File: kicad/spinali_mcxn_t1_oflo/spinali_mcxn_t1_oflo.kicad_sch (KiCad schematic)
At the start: 0 parts

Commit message: Added Rev-A in MR-MCXN-T1-OFLO
- Added Rev-A in schematic and layout
- Created production files

Signed-off-by: Youri Tils <youri.tils@nxp.com>
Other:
- company: NXP SEMICONDUCTORS B.V. -> ${COMPANY}
- title: MR-MCXN-T1-OFLO -> ${TITLE}
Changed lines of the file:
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@@
 	(paper "A4")
 	(title_block
-		(title "MR-MCXN-T1-OFLO")
-		(date "2025-04-16")
-		(rev "X0")
-		(company "NXP SEMICONDUCTORS B.V.")
-		(comment 3 "DESIGNER: YOURI TILS")
-		(comment 4 "CTO SYSTEM INNOVATIONS / MOBILE ROBOTICS DOMAIN")
+		(title "${TITLE}")
+		(date "2026-08-24")
+		(rev "${BOARD_REV}")
+		(company "${COMPANY}")
+		(comment 1 "DESIGNER: ${DESIGNER}")
+		(comment 2 "${DEPARTMENT}")
+		(comment 3 "REVIEWED BY: ${REVIEWER}")
 	)
 	(text "MR-MCXN-T1 Optical Flow"

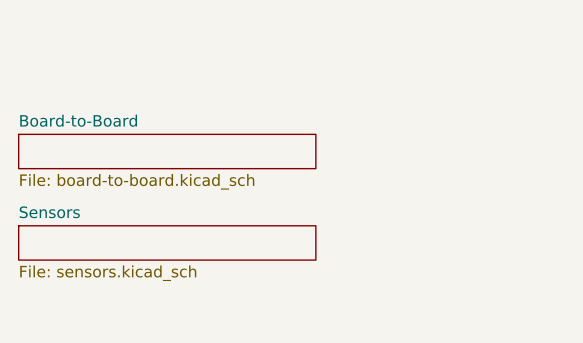
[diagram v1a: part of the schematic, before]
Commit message: Updated block diagrams of F9P, IO and OFLO boards
Signed-off-by: Youri Tils <youri.tils@nxp.com>
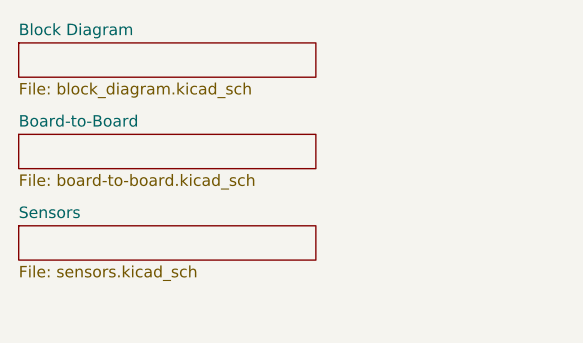
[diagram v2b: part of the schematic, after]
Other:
- added sheet Block Diagram (block_diagram.kicad_sch)
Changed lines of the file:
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@@
+	)
+	(sheet
+		(at 29.21 36.83)
+		(size 33.02 3.81)
+		(exclude_from_sim no)
+		(in_bom yes)
+		(on_board yes)
+		(dnp no)
+		(fields_autoplaced yes)
+		(stroke
+			(width 0.1524)
+			(type solid)
+		)
+		(fill
+			(color 0 0 0 0.0000)
+		)
+		(property "Sheetname" "Block Diagram"
+			(at 29.21 36.1184 0)
+			(effects
+				(font
+					(size 1.27 1.27)
+				)
+				(justify left bottom)
+			)
+		)
+		(property "Sheetfile" "block_diagram.kicad_sch"
+			(at 29.21 41.2246 0)
+			(effects
+				(font
+					(size 1.27 1.27)
+				)
+				(justify left top)
+			)
+		)
+		(instances
+			(project "spinali_mcxn_t1_oflo"
+				(path "/04285d74-eeba-483c-9378-52bd287e15a2"
+					(page "4")
+				)
+			)
+		)
 	)
 	(sheet
